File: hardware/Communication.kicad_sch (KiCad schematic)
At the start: 28 parts, among them J1 Conn_01x04_Pin, J2 Conn_01x03_Male, J3 USB_C_Receptacle_USB2.0, U21 TXB0102DCT, U22 ADUM4160

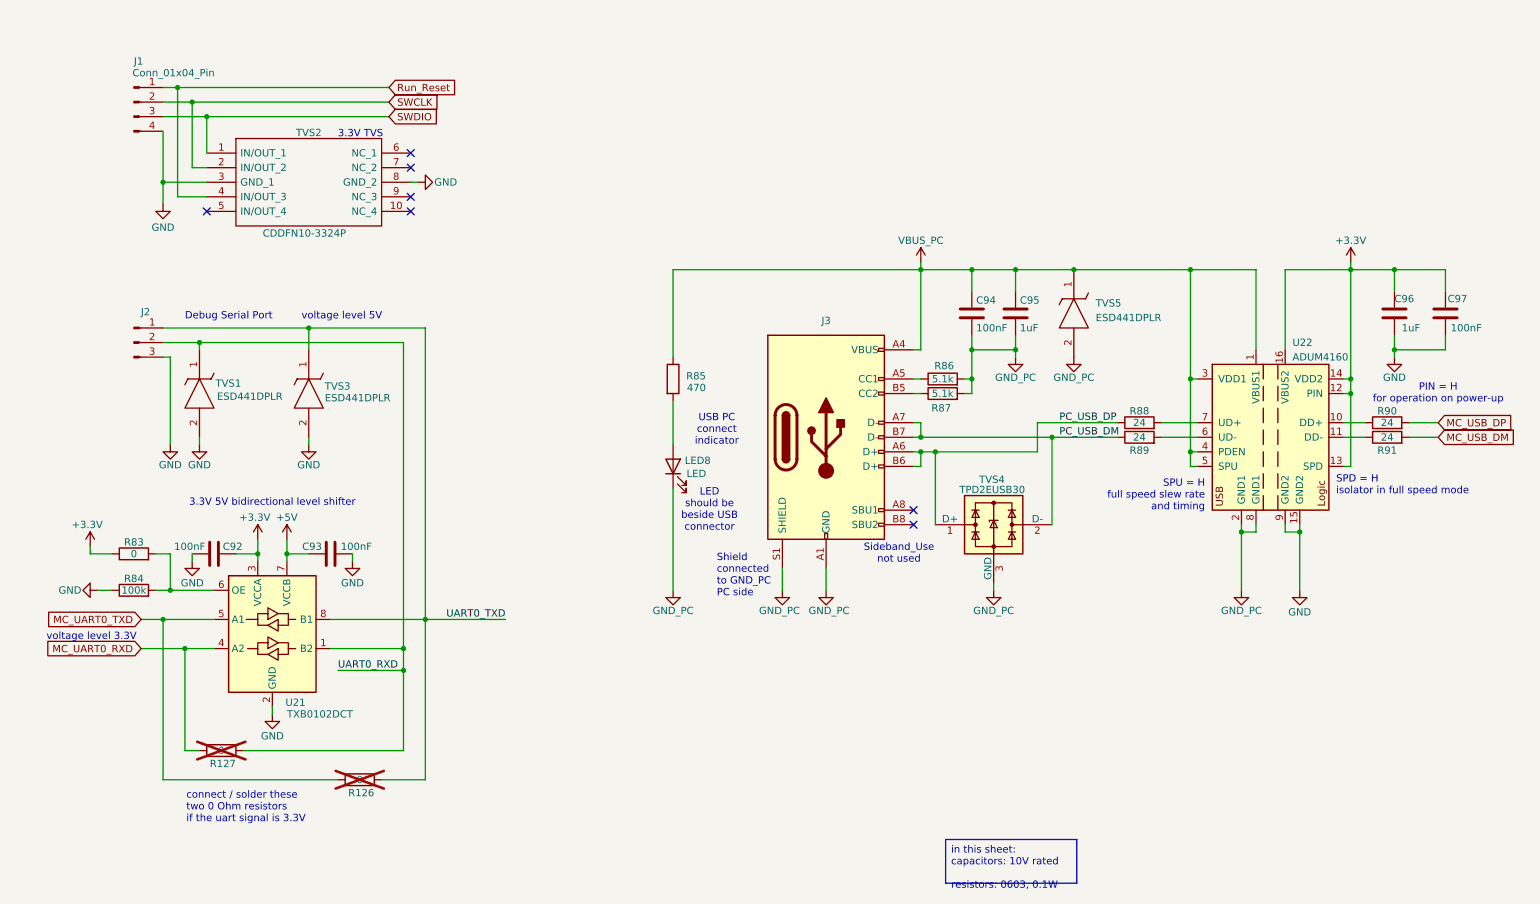
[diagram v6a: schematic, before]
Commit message: The part designators have been reannotated.
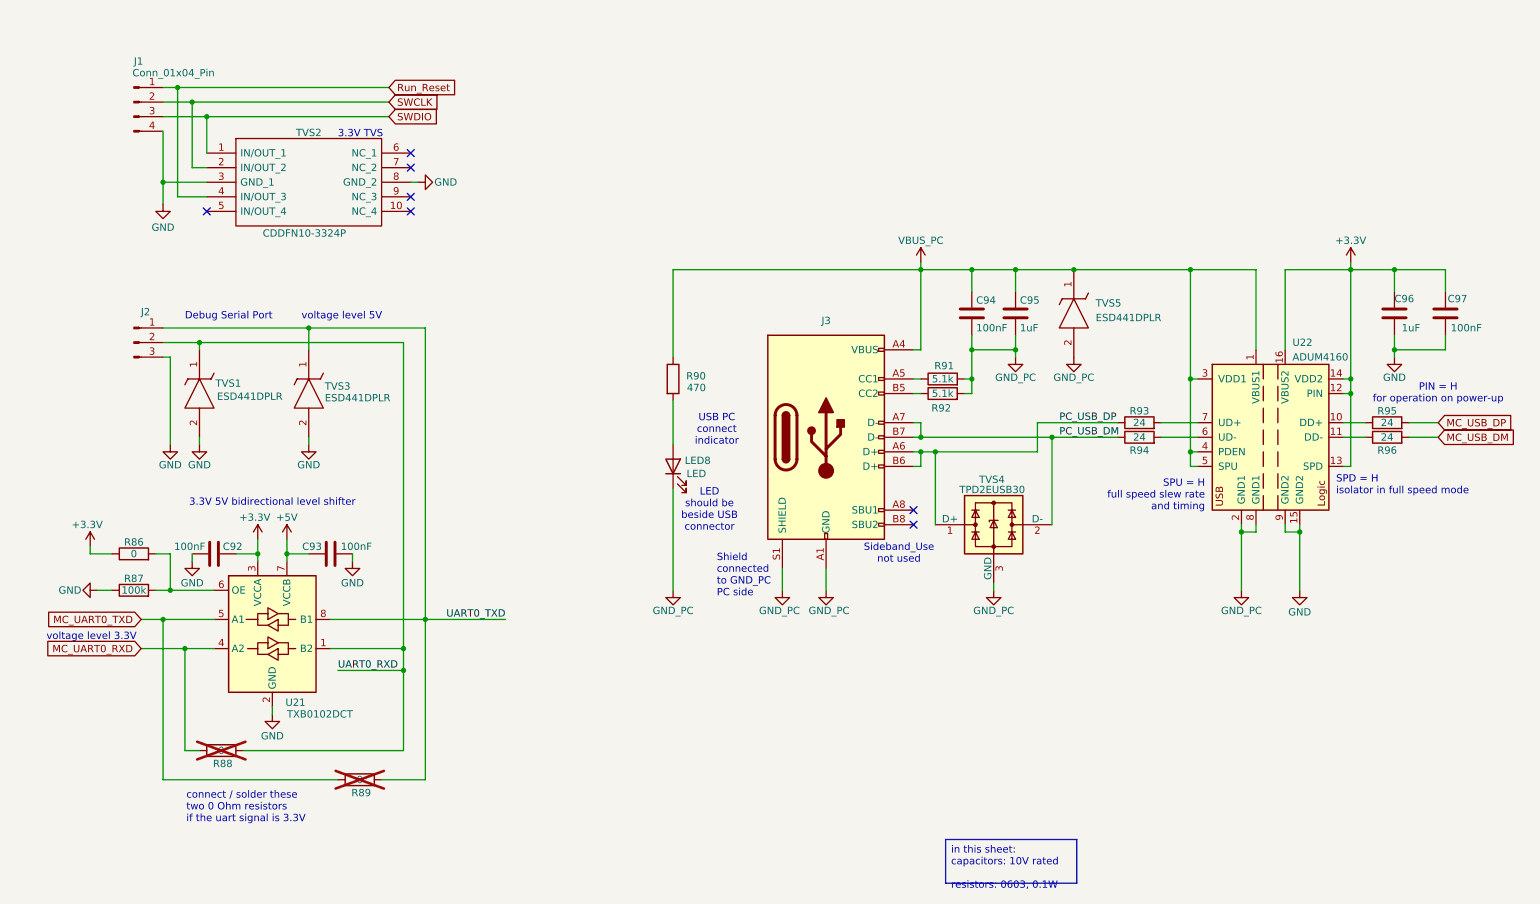
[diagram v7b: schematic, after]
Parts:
- renumbered R83 to R86, R84 to R87, R127 to R88, R126 to R89, R85 to R90, R86 to R91, R87 to R92, R88 to R93, R89 to R94, R90 to R95, R91 to R96
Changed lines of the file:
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@@
 		(on_board yes)
 		(dnp no)
-		(property "Reference" "R87"
+		(property "Reference" "R92"
 			(at 176.276 82.55 90)
 			(effects
@@
 			(project "harp.device.quad.dac"
 				(path "/6b47c519-21c4-43bd-9777-b273999e4447/08506a40-9943-41e4-b528-13f6a4c7e855"
-					(reference "R87")
+					(reference "R92")
 					(unit 1)
 				)
@@
 		(on_board yes)
 		(dnp no)
-		(property "Reference" "R91"
+		(property "Reference" "R96"
 			(at 254 89.916 90)
 			(effects
@@
 			(project "harp.device.quad.dac"
 				(path "/6b47c519-21c4-43bd-9777-b273999e4447/08506a40-9943-41e4-b528-13f6a4c7e855"
-					(reference "R91")
+					(reference "R96")
 					(unit 1)
 				)
@@
 		(on_board yes)
 		(dnp no)
-		(property "Reference" "R84"
+		(property "Reference" "R87"
 			(at 35.56 112.268 90)
 			(effects
@@
 			(project "harp.device.quad.dac"
 				(path "/6b47c519-21c4-43bd-9777-b273999e4447/08506a40-9943-41e4-b528-13f6a4c7e855"
-					(reference "R84")
+					(reference "R87")
 					(unit 1)
 				)
@@
 		(on_board yes)
 		(dnp no)
-		(property "Reference" "R89"
+		(property "Reference" "R94"
 			(at 210.82 89.916 90)
 			(effects
@@
 			(project "harp.device.quad.dac"
 				(path "/6b47c519-21c4-43bd-9777-b273999e4447/08506a40-9943-41e4-b528-13f6a4c7e855"
-					(reference "R89")
+					(reference "R94")
 					(unit 1)
 				)
@@
 		(on_board yes)
 		(dnp no)
-		(property "Reference" "R86"
+		(property "Reference" "R91"
 			(at 176.784 75.184 90)
 			(effects
@@
 			(project "harp.device.quad.dac"
 				(path "/6b47c519-21c4-43bd-9777-b273999e4447/08506a40-9943-41e4-b528-13f6a4c7e855"
-					(reference "R86")
+					(reference "R91")
 					(unit 1)
 				)
@@
 		(on_board no)
 		(dnp yes)
-		(property "Reference" "R126"
+		(property "Reference" "R89"
 			(at 75.184 149.606 90)
 			(effects
@@
 			(project "harp.device.quad.dac"
 				(path "/6b47c519-21c4-43bd-9777-b273999e4447/08506a40-9943-41e4-b528-13f6a4c7e855"
-					(reference "R126")
+					(reference "R89")
 					(unit 1)
 				)
@@
 		(on_board yes)
 		(dnp no)
-		(property "Reference" "R83"
+		(property "Reference" "R86"
 			(at 35.56 105.918 90)
 			(effects
@@
 			(project "harp.device.quad.dac"
 				(path "/6b47c519-21c4-43bd-9777-b273999e4447/08506a40-9943-41e4-b528-13f6a4c7e855"
-					(reference "R83")
+					(reference "R86")
 					(unit 1)
 				)
@@
 		(on_board no)
 		(dnp yes)
-		(property "Reference" "R127"
+		(property "Reference" "R88"
 			(at 51.054 144.526 90)
 			(effects
@@
 			(project "harp.device.quad.dac"
 				(path "/6b47c519-21c4-43bd-9777-b273999e4447/08506a40-9943-41e4-b528-13f6a4c7e855"
-					(reference "R127")
+					(reference "R88")
 					(unit 1)
 				)
@@
 		(on_board yes)
 		(dnp no)
-		(property "Reference" "R90"
+		(property "Reference" "R95"
 			(at 254 83.058 90)
 			(effects
@@
 			(project "harp.device.quad.dac"
 				(path "/6b47c519-21c4-43bd-9777-b273999e4447/08506a40-9943-41e4-b528-13f6a4c7e855"
-					(reference "R90")
+					(reference "R95")
 					(unit 1)
 				)
@@
 		(on_board yes)
 		(dnp no)
-		(property "Reference" "R85"
+		(property "Reference" "R90"
 			(at 131.826 76.962 0)
 			(effects
@@
 			(project "harp.device.quad.dac"
 				(path "/6b47c519-21c4-43bd-9777-b273999e4447/08506a40-9943-41e4-b528-13f6a4c7e855"
-					(reference "R85")
+					(reference "R90")
 					(unit 1)
 				)
@@
 		(on_board yes)
 		(dnp no)
-		(property "Reference" "R88"
+		(property "Reference" "R93"
 			(at 210.82 83.058 90)
 			(effects
@@
 			(project "harp.device.quad.dac"
 				(path "/6b47c519-21c4-43bd-9777-b273999e4447/08506a40-9943-41e4-b528-13f6a4c7e855"
-					(reference "R88")
+					(reference "R93")
 					(unit 1)
 				)
